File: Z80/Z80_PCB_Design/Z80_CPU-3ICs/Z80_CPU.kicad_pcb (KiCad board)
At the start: 2 copper layers, 95 x 95 mm, 47 parts, among them J1 USB_B, J2 Conn_01x12, J3 Conn_01x12, J4 Conn_01x02, U1 Z80CPU, U2 AS6C4008, U3 4.9152 MHz, U4 CY8C5267AXI-LP051, U5 MCP23017_SP, Y1 32.768KHz

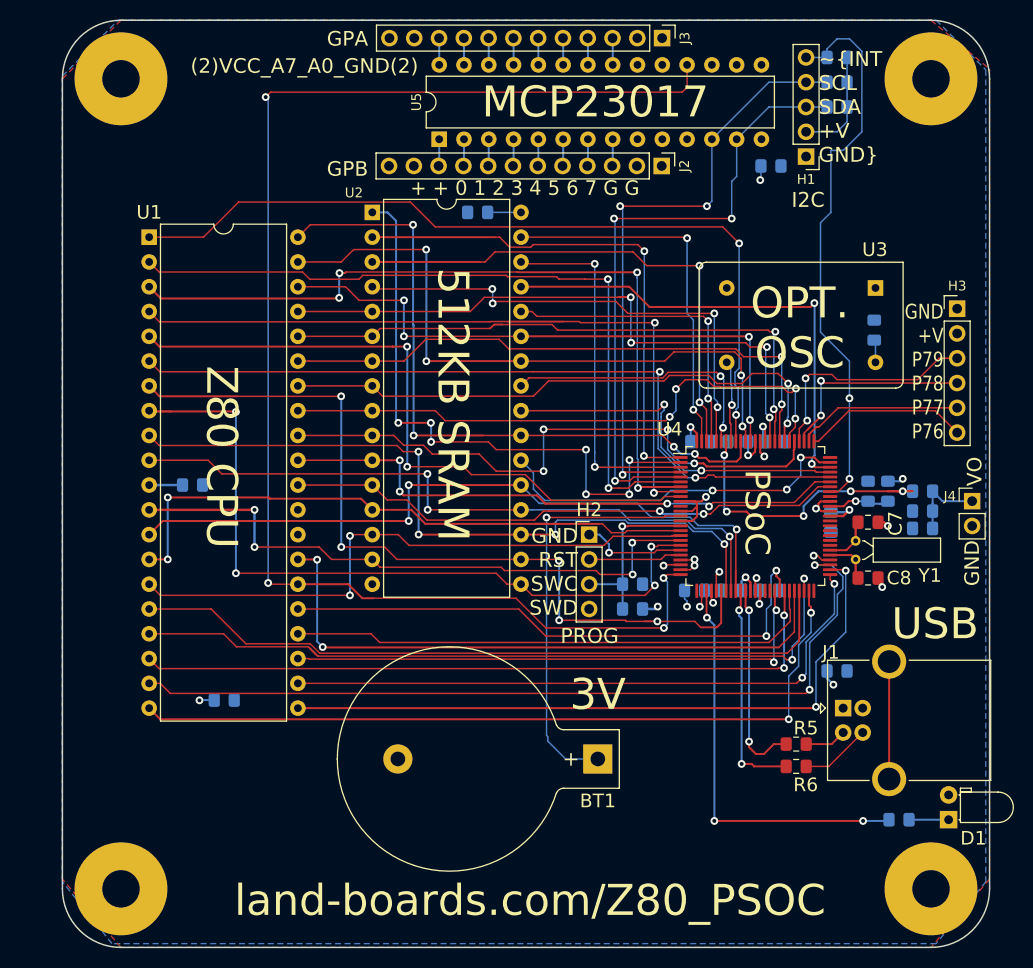
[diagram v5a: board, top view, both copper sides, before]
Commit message: Got external 512KB SRAM working
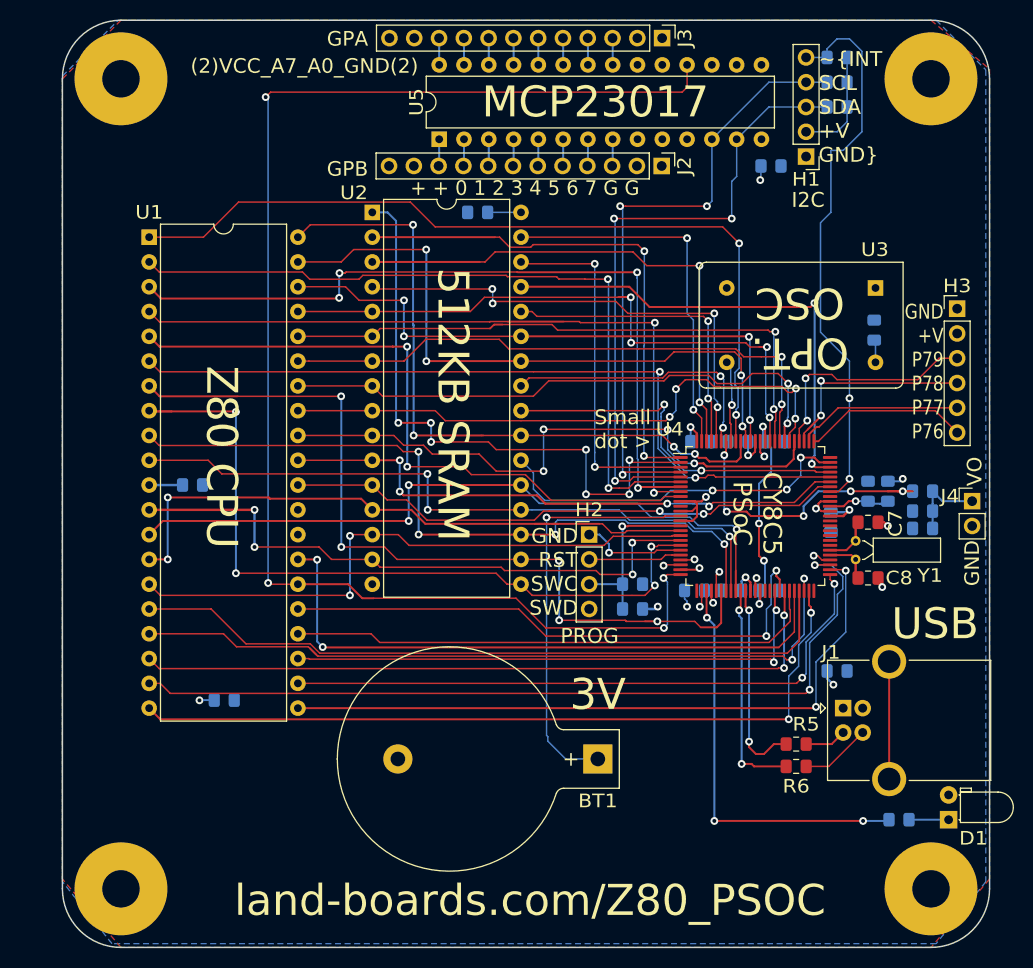
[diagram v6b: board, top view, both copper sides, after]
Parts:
- C16: value 10pF -> 0.001uF
- C7, C8: value 10pF -> 8pF
- D1: value LED_Small_ALT -> LED
- R9: value 2.2K -> 100
- renumbered MTG?1 to MTG4
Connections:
- C3 pad 1: Net-(C3-Pad1) -> Net-(C2-Pad1)
- U4 pad 86: Net-(C3-Pad1) -> Net-(C2-Pad1)
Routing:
- net Net-(C2-Pad1): track 2.78 -> 22.5 mm, vias 1 -> 4
- net Net-(C3-Pad1): track 3.24 -> 0.00 mm, vias 1 -> 0
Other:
- board text added: "CY8C5 PSoC"
- board text added: "REV 2"
- board text added: "Small dot >"
- board text removed: "PSoC"

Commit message: Test all 512KB - working
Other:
- board text added: "A0 GND ~REF ~M1 ~RST ~BREQ ~WAIT ~BACK ~CPUWR ~CPURD"
- board text added: "A10 A9 A8 A7 A6 A5 A4 A3 A2 A1"
- board text added: "A11 A12 A13 A14 A15 CLK"
- board text added: "D0 D1 ~INT ~NMI ~HALT ~MREQ ~IORQ"
- board text added: "D4 D3 D5 D6 5V D2 D7"
- board text added: "SWD SWC ~RST GND"
- board text added: "~RD ~CS"
- board text added: "~WR"
- board text removed: "GND RST SWC SWD"
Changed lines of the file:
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@@
   (general
     (thickness 1.6)
-    (drawings 31)
-    (tracks 1152)
+    (drawings 38)
+    (tracks 1150)
     (zones 0)
     (modules 47)
@@
     (descr "Through hole straight pin header, 1x05, 2.54mm pitch, single row")
     (tags "Through hole pin header THT 1x05 2.54mm single row")
-    (fp_text reference H1 (at 0 -2.33 180) (layer F.SilkS)
+    (fp_text reference H1 (at 2.54 -0.127 180) (layer F.SilkS)
       (effects (font (size 1.397 1.524) (thickness 0.254)))
     )
@@
     )
   )
+  (gr_text "~RD\n\n~CS" (at 48.387 42.672) (layer F.SilkS)
+    (effects (font (size 1.4478 1.524) (thickness 0.34925)) (justify left))
+  )
+  (gr_text ~WR (at 48.133 27.305) (layer F.SilkS)
+    (effects (font (size 1.4478 1.524) (thickness 0.34925)) (justify left))
+  )
+  (gr_text "A0\nGND\n~REF\n~M1\n~RST\n~BREQ\n~WAIT\n~BACK\n~CPUWR\n~CPURD" (at 25.273 59.055) (layer F.SilkS)
+    (effects (font (size 1.4478 1.524) (thickness 0.34925)) (justify left))
+  )
+  (gr_text "A10\nA9\nA8\nA7\nA6\nA5\nA4\nA3\nA2\nA1" (at 25.273 33.782) (layer F.SilkS)
+    (effects (font (size 1.4478 1.524) (thickness 0.34925)) (justify left))
+  )
+  (gr_text "D0\nD1\n~INT\n~NMI\n~HALT\n~MREQ\n~IORQ" (at 7.493 62.992) (layer F.SilkS)
+    (effects (font (size 1.4478 1.524) (thickness 0.34925)) (justify right))
+  )
+  (gr_text "D4\nD3\nD5\nD6\n5V\nD2\nD7" (at 7.62 45.085) (layer F.SilkS)
+    (effects (font (size 1.4478 1.524) (thickness 0.34925)) (justify right))
+  )
+  (gr_text "A11\nA12\nA13\nA14\nA15\nCLK" (at 7.62 28.575) (layer F.SilkS)
+    (effects (font (size 1.4478 1.524) (thickness 0.34925)) (justify right))
+  )
   (gr_text "REV 2" (at 67.056 89.662) (layer B.SilkS)
     (effects (font (size 3.175 3.175) (thickness 0.79375)) (justify mirror))
@@
     (effects (font (size 1.524 1.27) (thickness 0.3175)) (justify right))
   )
-  (gr_text PROG (at 57.0103 63.0936) (layer F.SilkS)
-    (effects (font (size 1.524 1.524) (thickness 0.381)) (justify right))
-  )
-  (gr_text "GND\nRST\nSWC\nSWD" (at 52.832 56.5277) (layer F.SilkS)
+  (gr_text PROG (at 59.309 63.627) (layer F.SilkS)
+    (effects (font (size 2.54 2.54) (thickness 0.635)) (justify right))
+  )
+  (gr_text "SWD\nSWC\n~RST\nGND\n" (at 52.832 56.5277) (layer F.SilkS)
     (effects (font (size 1.524 1.524) (thickness 0.381)) (justify right))
   )
@@
     (effects (font (size 3.175 3.175) (thickness 0.79375)))
   )
-  (gr_text I2C (at 78.105 18.415) (layer F.SilkS)
-    (effects (font (size 1.524 1.524) (thickness 0.381)) (justify right))
+  (gr_text I2C (at 80.137 17.78) (layer F.SilkS)
+    (effects (font (size 2.54 2.54) (thickness 0.635)) (justify right))
   )
   (gr_text "~INT\nSCL\nSDA\n+V\nGND" (at 77.47 8.89) (layer F.SilkS)
@@
     (effects (font (size 1.905 1.905) (thickness 0.47625)))
   )
-  (gr_text "512KB SRAM" (at 40.005 39.37 270) (layer F.SilkS)
+  (gr_text "512KB  SRAM" (at 40.005 39.37 270) (layer F.SilkS)
     (effects (font (size 3.175 3.175) (thickness 0.79375)))
   )
-  (gr_text "Z80 CPU" (at 16.30426 44.7675 270) (layer F.SilkS)
+  (gr_text "Z80   CPU" (at 16.256 46.228 270) (layer F.SilkS)
     (effects (font (size 3.175 3.175) (thickness 0.79375)))
   )
@@
   (segment (start 85.861 47.235) (end 86.106 46.99) (width 0.2032) (layer B.Cu) (net 2))
   (via (at 49.6062 50.946999) (size 0.8) (drill 0.4) (layers F.Cu B.Cu) (net 3))
-  (segment (start 54.864 75.692) (end 51.562 75.692) (width 0.1524) (layer B.Cu) (net 3) (status 10))
-  (segment (start 51.562 75.692) (end 49.7332 73.8632) (width 0.1524) (layer B.Cu) (net 3))
-  (segment (start 49.6062 73.279) (end 49.6062 50.946999) (width 0.1524) (layer B.Cu) (net 3))
-  (segment (start 49.7332 73.406) (end 49.6062 73.279) (width 0.1524) (layer B.Cu) (net 3))
-  (segment (start 49.7332 73.8632) (end 49.7332 73.406) (width 0.1524) (layer B.Cu) (net 3))
   (segment (start 50.171885 50.946999) (end 49.6062 50.946999) (width 0.1524) (layer F.Cu) (net 3))
   (segment (start 61.741999 50.8) (end 61.595 50.946999) (width 0.1524) (layer F.Cu) (net 3))
   (segment (start 63.3375 50.8) (end 61.741999 50.8) (width 0.1524) (layer F.Cu) (net 3))
   (segment (start 61.595 50.946999) (end 50.171885 50.946999) (width 0.1524) (layer F.Cu) (net 3))
+  (segment (start 52.1462 75.692) (end 49.6062 73.152) (width 0.2032) (layer B.Cu) (net 3))
+  (segment (start 54.864 75.692) (end 52.1462 75.692) (width 0.2032) (layer B.Cu) (net 3))
+  (segment (start 49.6062 73.152) (end 49.6062 50.946999) (width 0.2032) (layer B.Cu) (net 3))
   (segment (start 57.395 60.325) (end 57.395 57.785) (width 0.2032) (layer B.Cu) (net 4) (status 30))
   (segment (start 53.975 57.785) (end 57.395 57.785) (width 0.2032) (layer B.Cu) (net 4) (status 30))

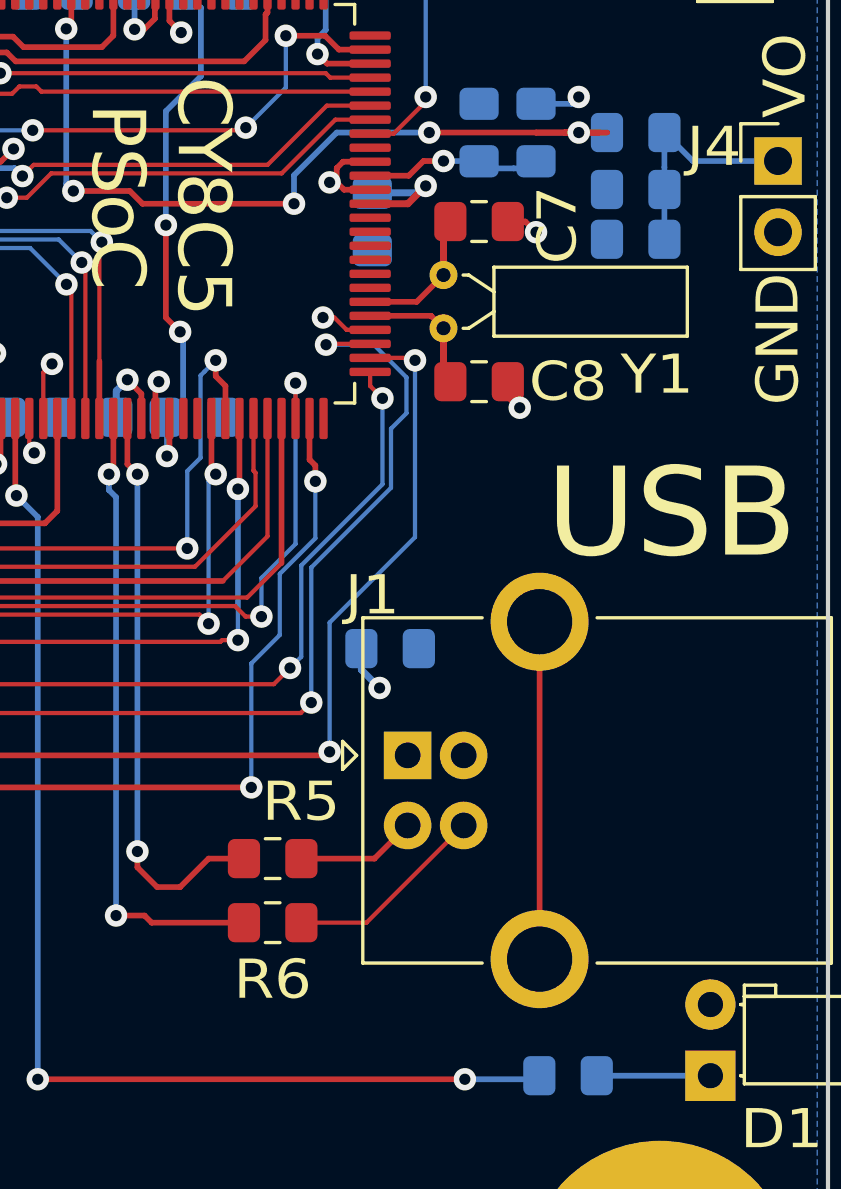
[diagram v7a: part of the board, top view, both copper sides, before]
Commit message: Front panel toggle on LED release
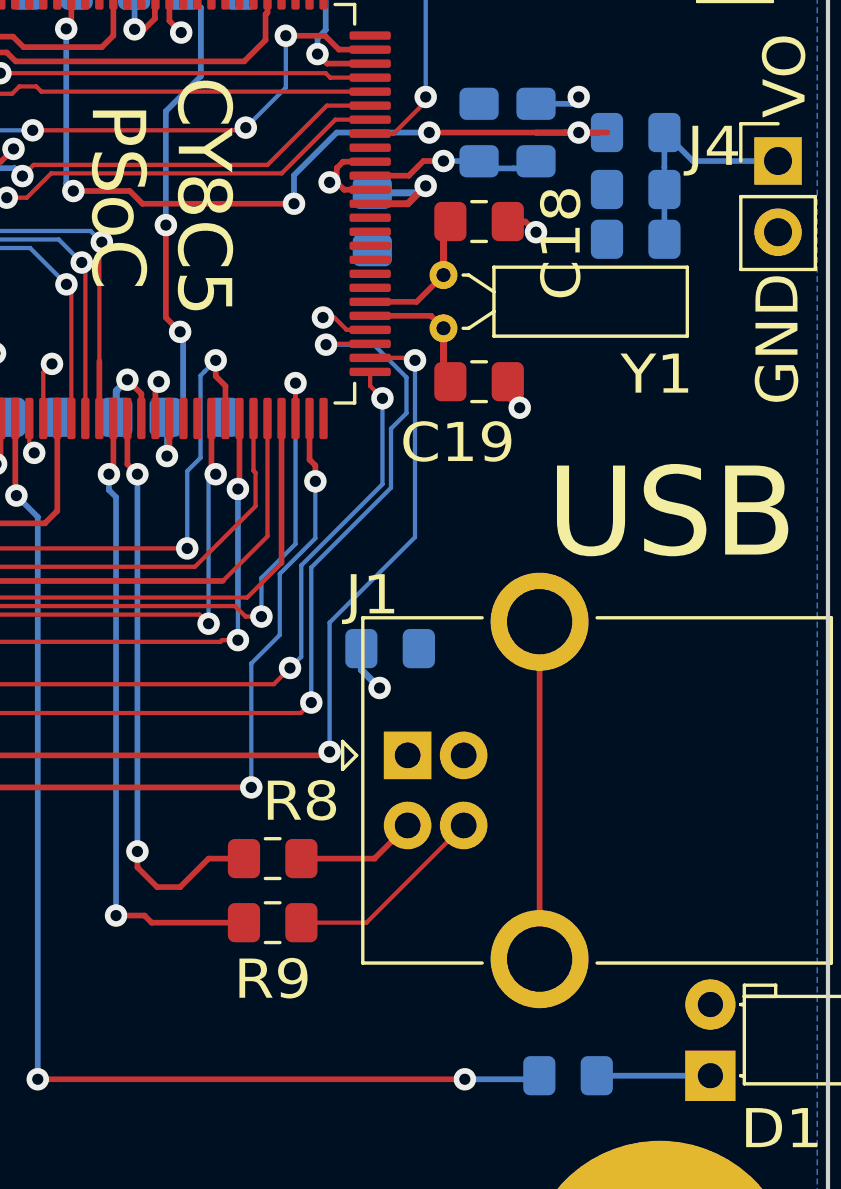
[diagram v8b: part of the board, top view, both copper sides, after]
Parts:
- renumbered C15 to C1, C2 to C10, C18 to C11, C9 to C12, C1 to C13, C11 to C14, C10 to C15, C6 to C16, C7 to C18, C8 to C19, C13 to C2, C14 to C3, C3 to C4, C17 to C5, C12 to C6, C4 to C7, C5 to C8, C16 to C9, R3 to R1, R1 to R3, R8 to R4, R9 to R5, R4 to R6, R5 to R8, R6 to R9
